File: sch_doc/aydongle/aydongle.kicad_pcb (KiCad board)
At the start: 2 copper layers, 51 parts, among them J1 prog, J2 USB_A, J3 Display, J4 Audio-Jack-3, Q1 Q_Photo_NPN_EC, Q2 Q_Photo_NPN_CE, U1 AP1117-33, U2 STM32F103C8TxSmall, U3 YM2149F, U4 LM4811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

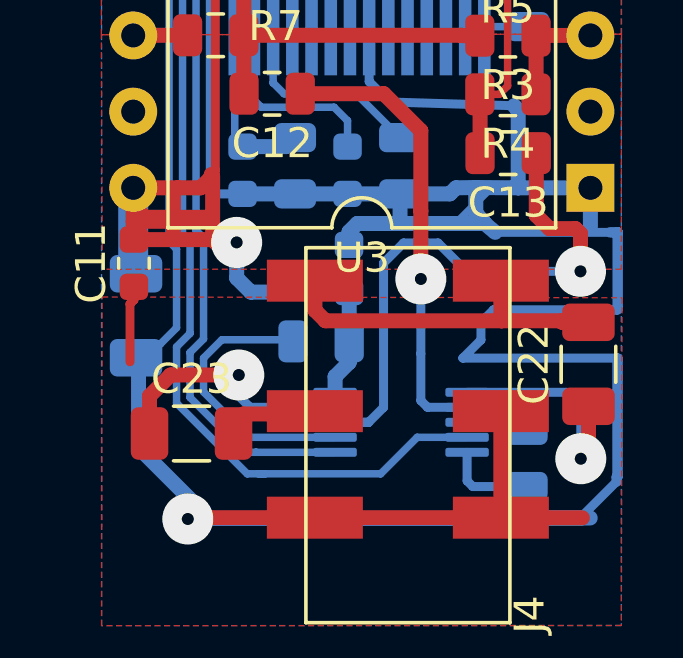
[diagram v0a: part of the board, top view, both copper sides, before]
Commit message: работает чип и усилитель
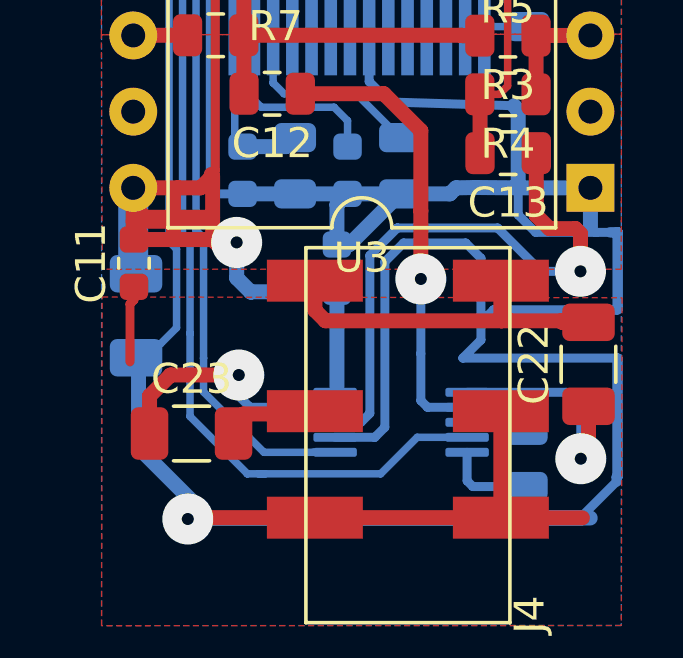
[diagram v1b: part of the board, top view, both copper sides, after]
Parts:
- removed R12: 100k, Resistor_SMD:R_0805_2012Metric
- moved C20 0.40 mm to (93.8, 126.7)
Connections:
- U4 pad 7: Net-(R12-Pad2) -> GND
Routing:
- net Net-(R12-Pad2): track 9.40 -> 0.00 mm
- net GND: track 400.9 -> 407.6 mm
- net +5V: track 82.4 -> 81.5 mm
- net /A_UPDN: track 44.6 -> 43.8 mm
